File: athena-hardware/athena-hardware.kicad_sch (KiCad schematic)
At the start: 13 parts, among them J1 LIPO BATTERY, SW1 SW_Push, SW2 SW_SPST, U1 TP4056, U2 NODEMCU, U3 MICRO-SD MODULE, U4 NEO6M-GPS-MODULE, U5 0.96" OLED

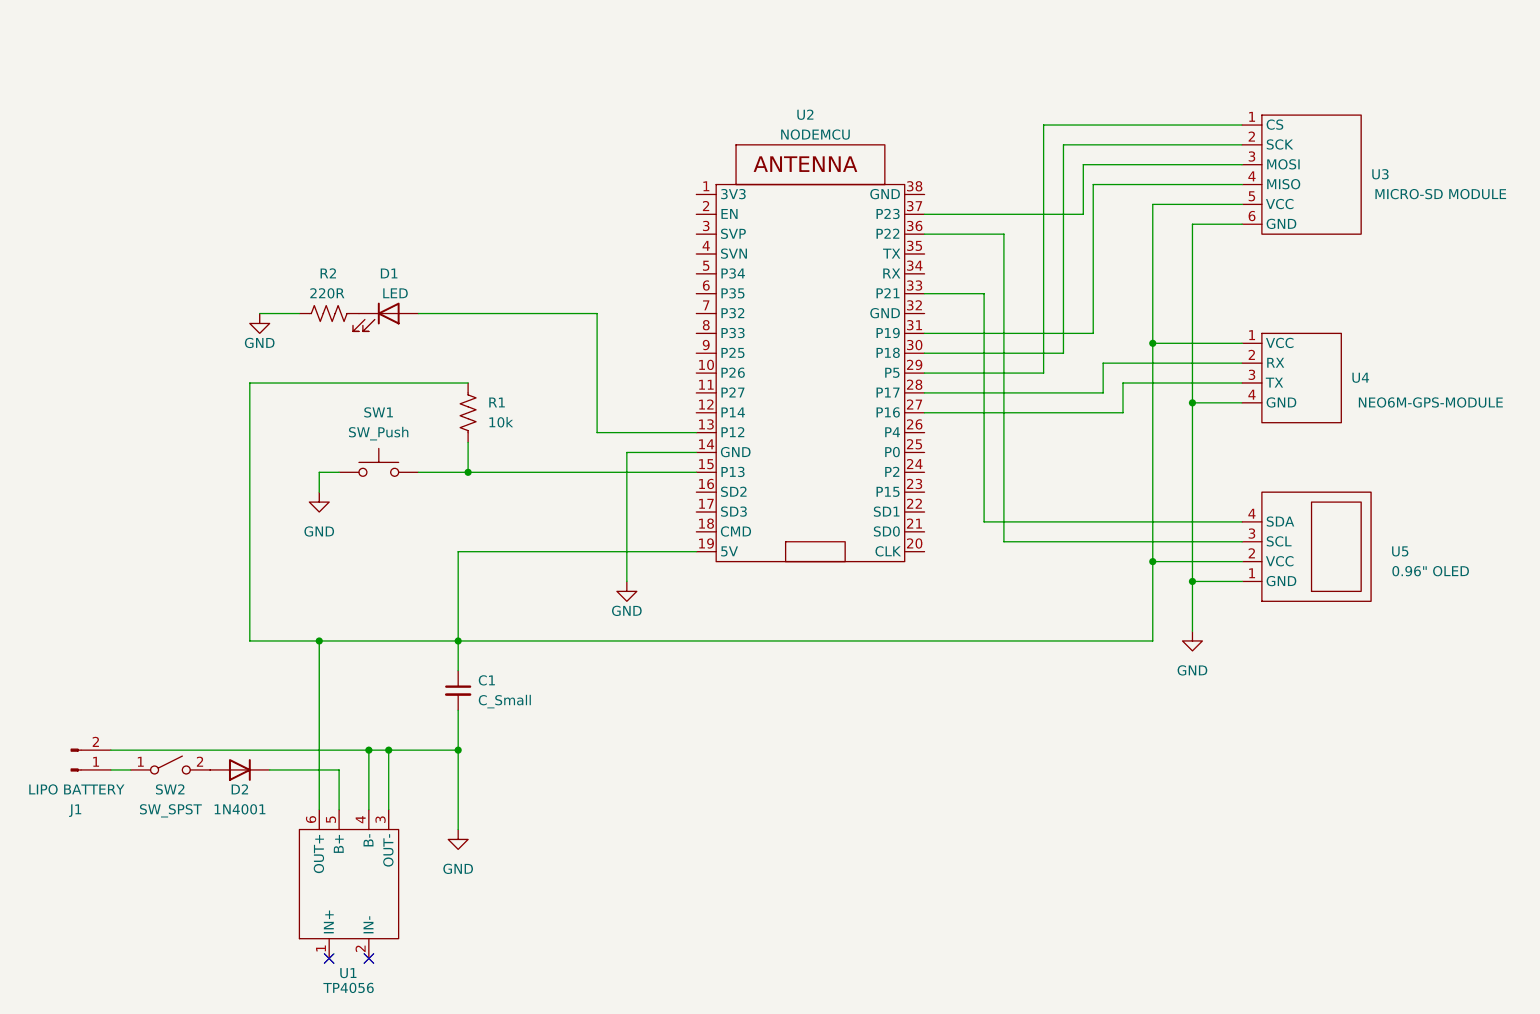
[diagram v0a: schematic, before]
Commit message: adds 3D design files
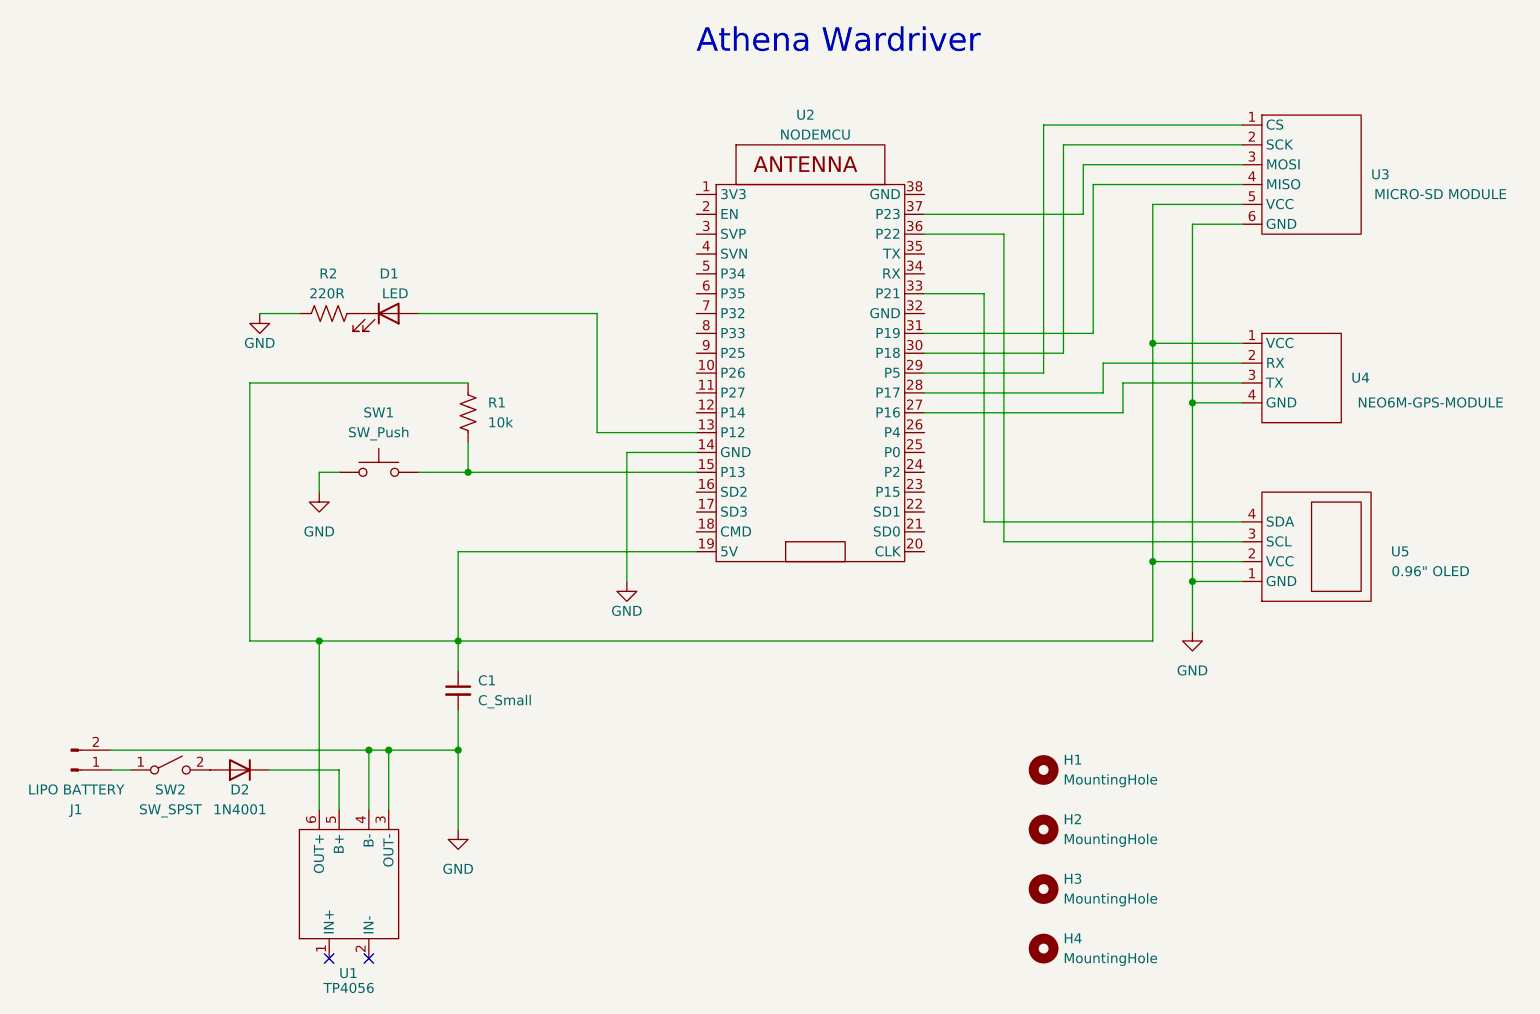
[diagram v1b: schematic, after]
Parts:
- added H1, H2, H3, H4: MountingHole, MountingHole:MountingHole_2.5mm, symbol Mechanical:MountingHole
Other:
- note added: "Athena Wardriver"
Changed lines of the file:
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@@
     (stroke (width 0) (type default))
+  )
+  (text "Athena Wardriver\n" (at 142.24 35.56 0)
+    (effects (font (face "Bookman Old Style") (size 3 3)) (justify left bottom))
   )
   (symbol (lib_id "Switch:SW_SPST") (at 74.93 127 0) (unit 1)
@@
         (path "/d4feba36-4703-475a-a98b-ed1ee1cd3c50"
           (reference "#PWR03") (unit 1)
+        )
+      )
+    )
+  )
+  (symbol (lib_id "Mechanical:MountingHole") (at 186.69 142.24 0) (unit 1)
+    (in_bom yes) (on_board yes) (dnp no) (fields_autoplaced)
+    (property "Reference" "H3" (at 189.23 140.97 0)
+      (effects (font (size 1.27 1.27)) (justify left))
+    )
+    (property "Value" "MountingHole" (at 189.23 143.51 0)
+      (effects (font (size 1.27 1.27)) (justify left))
+    )
+    (property "Footprint" "MountingHole:MountingHole_2.5mm" (at 186.69 142.24 0)
+      (effects (font (size 1.27 1.27)) hide)
+    )
+    (property "Datasheet" "~" (at 186.69 142.24 0)
+      (effects (font (size 1.27 1.27)) hide)
+    )
+    (instances
+      (project "athena-hardware"
+        (path "/d4feba36-4703-475a-a98b-ed1ee1cd3c50"
+          (reference "H3") (unit 1)
         )
       )
@@
         (path "/d4feba36-4703-475a-a98b-ed1ee1cd3c50"
           (reference "U3") (unit 1)
+        )
+      )
+    )
+  )
+  (symbol (lib_id "Mechanical:MountingHole") (at 186.69 127 0) (unit 1)
+    (in_bom yes) (on_board yes) (dnp no) (fields_autoplaced)
+    (property "Reference" "H1" (at 189.23 125.73 0)
+      (effects (font (size 1.27 1.27)) (justify left))
+    )
+    (property "Value" "MountingHole" (at 189.23 128.27 0)
+      (effects (font (size 1.27 1.27)) (justify left))
+    )
+    (property "Footprint" "MountingHole:MountingHole_2.5mm" (at 186.69 127 0)
+      (effects (font (size 1.27 1.27)) hide)
+    )
+    (property "Datasheet" "~" (at 186.69 127 0)
+      (effects (font (size 1.27 1.27)) hide)
+    )
+    (instances
+      (project "athena-hardware"
+        (path "/d4feba36-4703-475a-a98b-ed1ee1cd3c50"
+          (reference "H1") (unit 1)
         )
       )
@@
         )
       )
+    )
+  )
+  (symbol (lib_id "Mechanical:MountingHole") (at 186.69 134.62 0) (unit 1)
+    (in_bom yes) (on_board yes) (dnp no) (fields_autoplaced)
+    (property "Reference" "H2" (at 189.23 133.35 0)
+      (effects (font (size 1.27 1.27)) (justify left))
+    )
+    (property "Value" "MountingHole" (at 189.23 135.89 0)
+      (effects (font (size 1.27 1.27)) (justify left))
+    )
+    (property "Footprint" "MountingHole:MountingHole_2.5mm" (at 186.69 134.62 0)
+      (effects (font (size 1.27 1.27)) hide)
+    )
+    (property "Datasheet" "~" (at 186.69 134.62 0)
+      (effects (font (size 1.27 1.27)) hide)
+    )
+    (instances
+      (project "athena-hardware"
+        (path "/d4feba36-4703-475a-a98b-ed1ee1cd3c50"
+          (reference "H2") (unit 1)
+        )
+      )
+    )
+  )
+  (symbol (lib_id "Mechanical:MountingHole") (at 186.69 149.86 0) (unit 1)
+    (in_bom yes) (on_board yes) (dnp no) (fields_autoplaced)
+    (property "Reference" "H4" (at 189.23 148.59 0)
+      (effects (font (size 1.27 1.27)) (justify left))
+    )
+    (property "Value" "MountingHole" (at 189.23 151.13 0)
+      (effects (font (size 1.27 1.27)) (justify left))
+    )
+    (property "Footprint" "MountingHole:MountingHole_2.5mm" (at 186.69 149.86 0)
+      (effects (font (size 1.27 1.27)) hide)
+    )
+    (property "Datasheet" "~" (at 186.69 149.86 0)
+      (effects (font (size 1.27 1.27)) hide)
+    )
+    (instances
+      (project "athena-hardware"
+        (path "/d4feba36-4703-475a-a98b-ed1ee1cd3c50"
+          (reference "H4") (unit 1)
+        )
+      )
